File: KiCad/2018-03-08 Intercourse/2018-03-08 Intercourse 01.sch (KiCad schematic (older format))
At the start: 33 parts

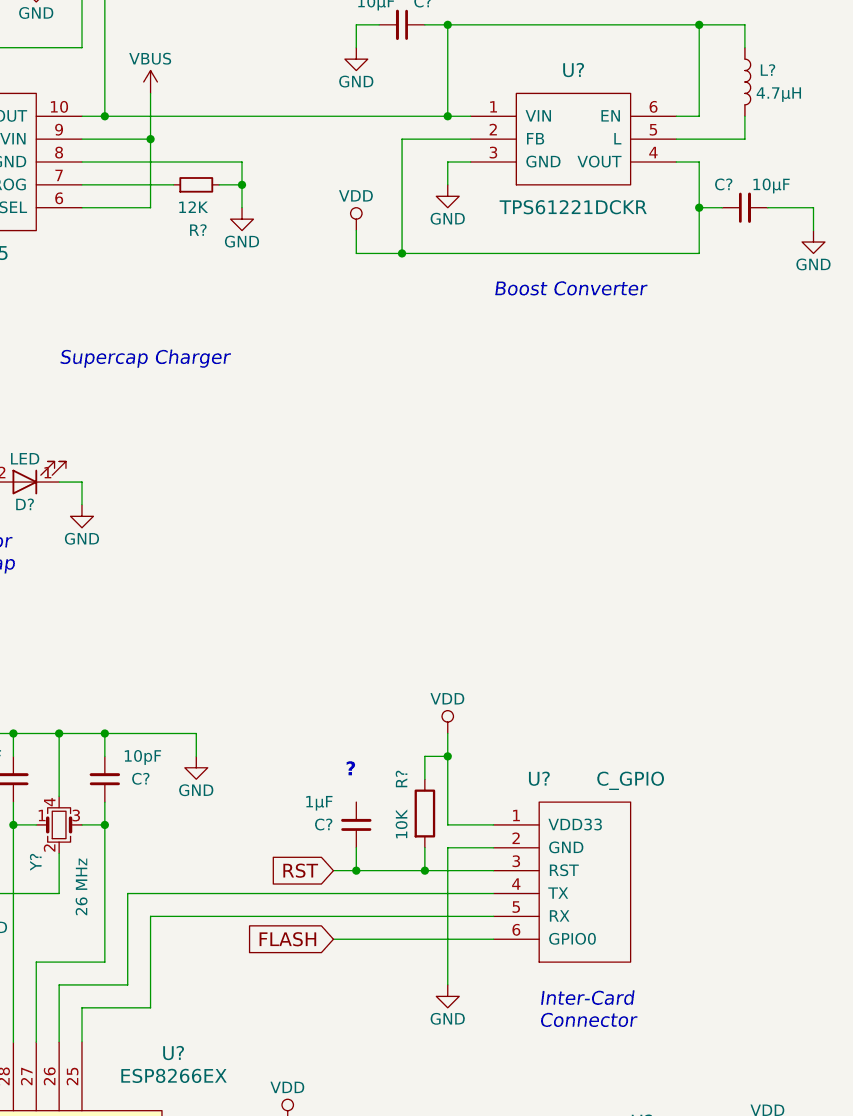
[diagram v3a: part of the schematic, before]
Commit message: added reset rc filter circuit
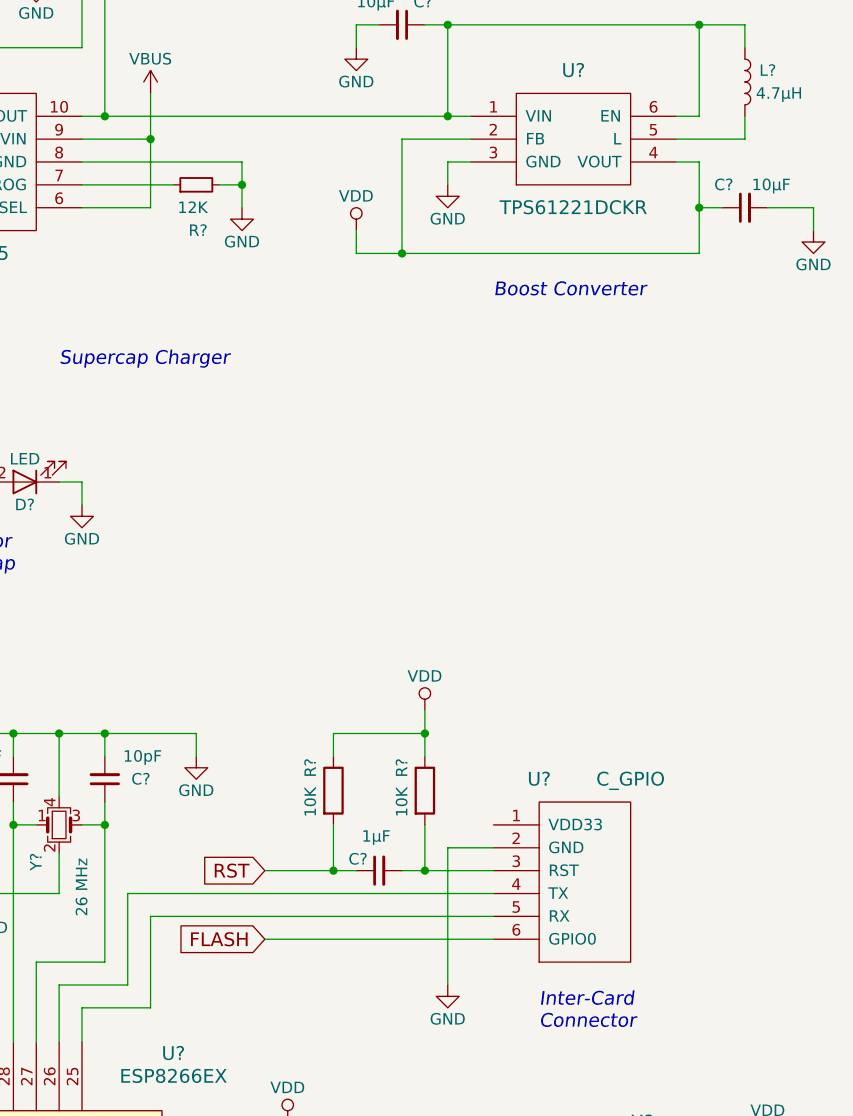
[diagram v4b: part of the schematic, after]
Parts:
- added R?: 10K, symbol R
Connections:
- net RST: now also R?.2; no longer R?.2, U?.3 (RST)
- net VDD: now also R?.1; no longer U?.1 (VDD33)
- net at C?.2: now also R?.2, U?.3 (RST)
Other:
- moved on the sheet: C?, R?
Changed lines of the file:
@@
 Text Notes 1400 6100 2    60   ~ 12
-?
-Text Notes 5200 5200 2    60   ~ 12
 ?
 $Comp
@@
 L VDD #PWR?
 U 1 1 5AB0F171
-P 5600 5000
-F 0 "#PWR?" H 5600 4850 50  0001 C CNN
-F 1 "VDD" H 5600 5150 50  0000 C CNN
-F 2 "" H 5600 5000 50  0001 C CNN
-F 3 "" H 5600 5000 50  0001 C CNN
-	1    5600 5000
+P 5500 4900
+F 0 "#PWR?" H 5500 4750 50  0001 C CNN
+F 1 "VDD" H 5500 5050 50  0000 C CNN
+F 2 "" H 5500 4900 50  0001 C CNN
+F 3 "" H 5500 4900 50  0001 C CNN
+	1    5500 4900
 	1    0    0    -1
 $EndComp
@@
 L R R?
 U 1 1 5AB249C6
-P 5500 5350
-F 0 "R?" V 5400 5500 50  0000 C CNN
-F 1 "10K" V 5400 5300 50  0000 C CNN
-F 2 "" V 5430 5350 50  0001 C CNN
-F 3 "" H 5500 5350 50  0001 C CNN
-	1    5500 5350
+P 5500 5250
+F 0 "R?" V 5400 5350 50  0000 C CNN
+F 1 "10K" V 5400 5200 50  0000 C CNN
+F 2 "" V 5430 5250 50  0001 C CNN
+F 3 "" H 5500 5250 50  0001 C CNN
+	1    5500 5250
 	1    0    0    -1
 $EndComp
@@
 L C_Small C?
 U 1 1 5AB287B2
-P 5200 5400
-F 0 "C?" H 5300 5400 50  0000 L CNN
-F 1 "1μF" H 5300 5300 50  0000 L CNN
-F 2 "" H 5200 5400 50  0001 C CNN
-F 3 "" H 5200 5400 50  0001 C CNN
-	1    5200 5400
-	-1   0    0    1
+P 5300 5600
+F 0 "C?" V 5350 5650 50  0000 L CNN
+F 1 "1μF" V 5450 5550 50  0000 L CNN
+F 2 "" H 5300 5600 50  0001 C CNN
+F 3 "" H 5300 5600 50  0001 C CNN
+	1    5300 5600
+	0    -1   -1   0
 $EndComp
 Wire Wire Line
@@
 	6600 2500 6700 2500
 Wire Wire Line
-	6700 2900 6700 2700
-Wire Wire Line
-	6700 2700 6700 2500
-Wire Wire Line
-	5200 2900 5400 2900
-Wire Wire Line
-	5400 2900 6700 2900
+	6700 2500 6700 2700
+Wire Wire Line
+	6700 2700 6700 2900
+Wire Wire Line
+	6700 2900 5400 2900
+Wire Wire Line
+	5400 2900 5200 2900
 Wire Wire Line
 	5400 2900 5400 2400
@@
 	4200 6100 3900 6100
 Wire Wire Line
-	5600 5400 5800 5400
-Wire Wire Line
 	5600 5500 5800 5500
-Wire Wire Line
-	5100 5600 5200 5600
-Wire Wire Line
-	5200 5600 5500 5600
-Wire Wire Line
-	5500 5600 5800 5600
 Wire Wire Line
 	4200 5700 4200 6100
@@
 	1100 3700 1100 3800
 Wire Wire Line
-	5600 5000 5600 5100
-Wire Wire Line
-	5600 5100 5600 5400
-Wire Wire Line
 	1100 5700 1100 5600
 Wire Wire Line
@@
 	3400 5000 3400 5200
 Wire Wire Line
-	5100 5900 5800 5900
+	4800 5900 5800 5900
 Wire Wire Line
 	4500 5000 4500 5100
@@
 Connection ~ 3200 5700
 Wire Wire Line
-	5200 5600 5200 5500
-Connection ~ 5200 5600
-Wire Wire Line
-	5500 5200 5500 5100
-Wire Wire Line
-	5500 5100 5600 5100
-Connection ~ 5600 5100
-Wire Wire Line
-	5500 5500 5500 5600
-Connection ~ 5500 5600
+	5500 4900 5500 5000
+Wire Wire Line
+	5500 5000 5500 5100
+Wire Wire Line
+	5500 5400 5500 5600
 Wire Wire Line
 	3500 6350 3500 6200
@@
 Text Notes 1400 9200 0    60   Italic 12
 Todo:\n* Status LEDs\n* USB Conn Check\n* Reset
-Text GLabel 5100 5900 0    60   Input ~ 0
+Text GLabel 4800 5900 0    60   Input ~ 0
 FLASH
-Text GLabel 5100 5600 0    60   Input ~ 0
+Text GLabel 4800 5600 0    60   Input ~ 0
 RST
 Text GLabel 4100 8100 2    60   Input ~ 0
@@
 Text GLabel 3300 6200 1    60   Input ~ 0
 RST
+$Comp
+L R R?
+U 1 1 5AB29192
+P 5100 5250
+F 0 "R?" V 5000 5350 50  0000 C CNN
+F 1 "10K" V 5000 5200 50  0000 C CNN
+F 2 "" V 5030 5250 50  0001 C CNN
+F 3 "" H 5100 5250 50  0001 C CNN
+	1    5100 5250
+	1    0    0    -1
+$EndComp
+Wire Wire Line
+	5100 5100 5100 5000
+Wire Wire Line
+	5100 5400 5100 5600
+Wire Wire Line
+	4800 5600 5100 5600
+Wire Wire Line
+	5100 5600 5200 5600
+Connection ~ 5100 5600
+Wire Wire Line
+	5400 5600 5500 5600
+Wire Wire Line
+	5500 5600 5800 5600
+Connection ~ 5500 5600
+Wire Wire Line
+	5100 5000 5500 5000
+Connection ~ 5500 5000
 $EndSCHEMATC

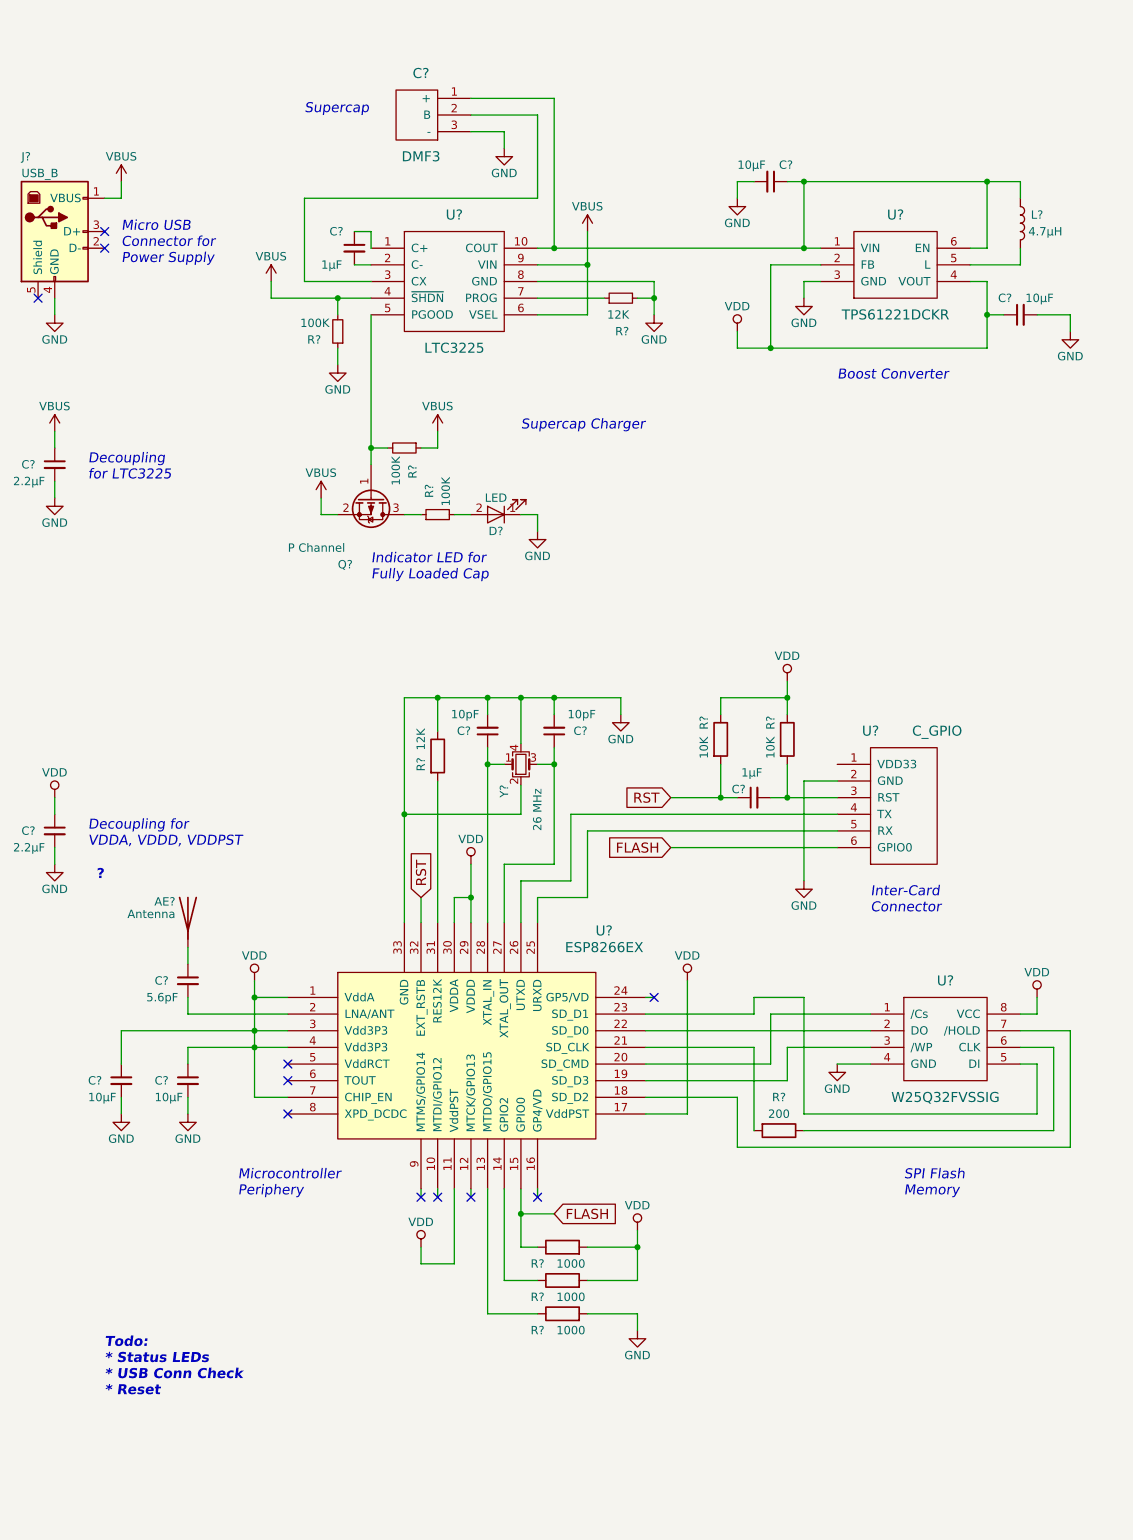
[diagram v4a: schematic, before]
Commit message: added leds to schematic
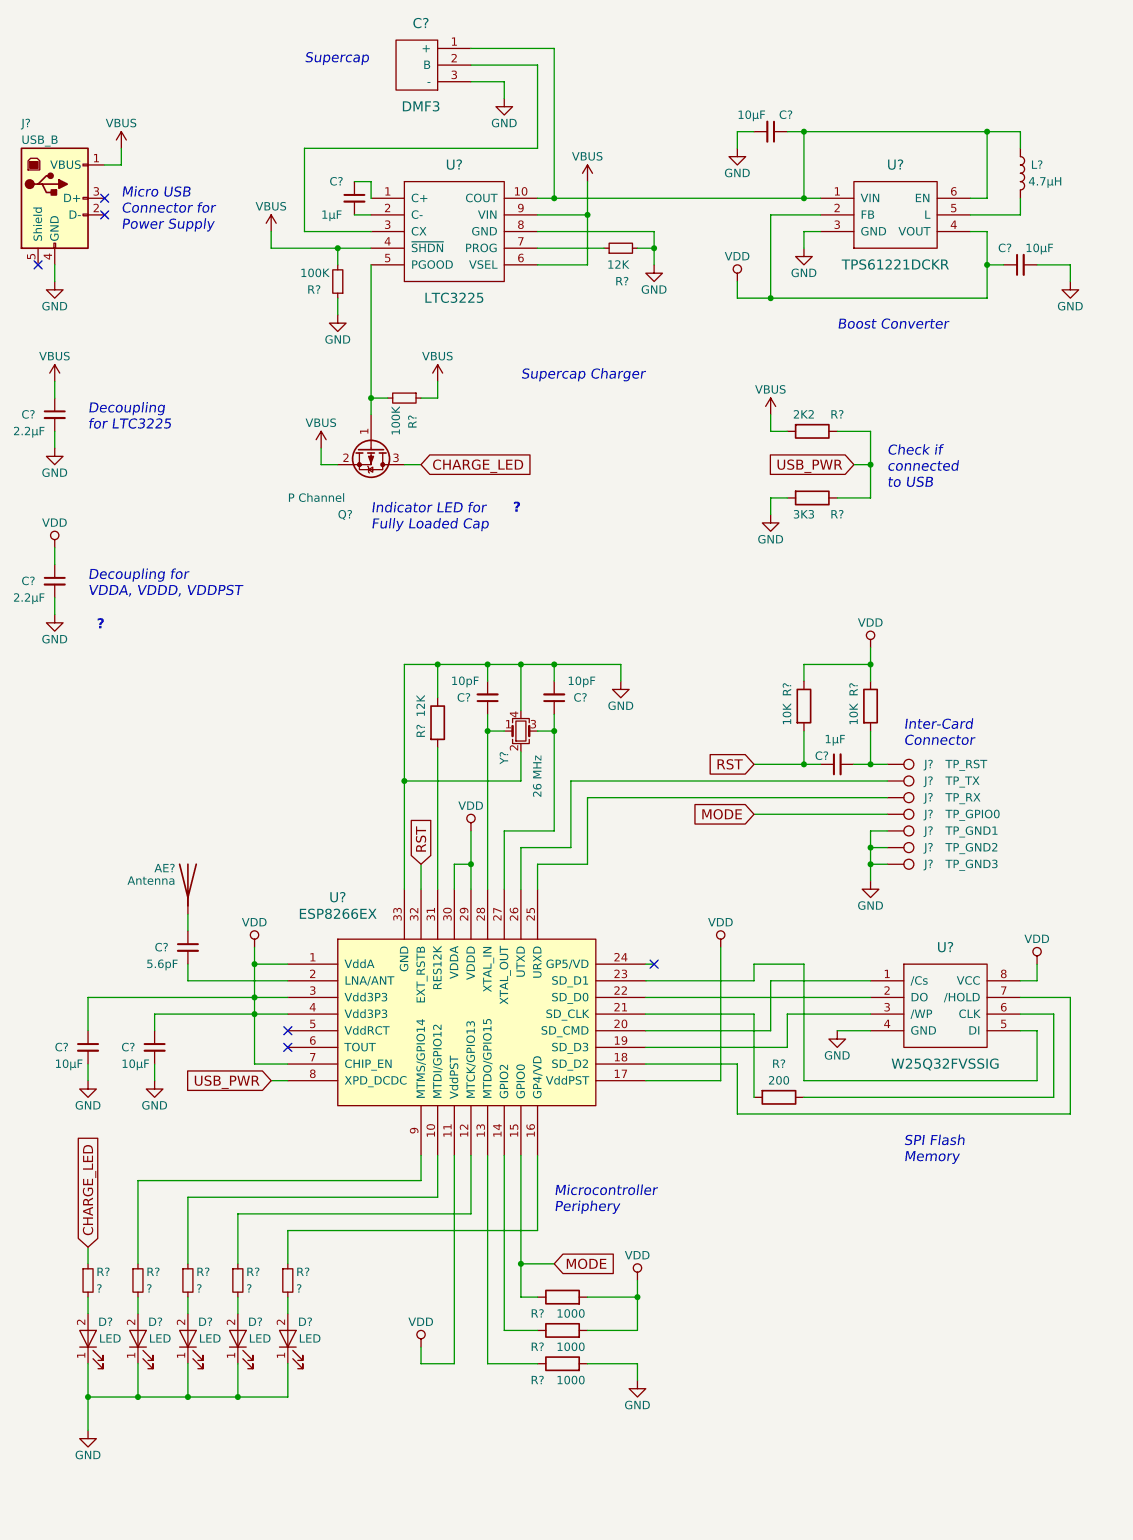
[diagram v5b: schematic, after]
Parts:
- removed U?: C_GPIO, symbol C_GPIO
- added D? (x4): LED, symbol LED
- added J?: TP_TX, symbol TEST_1P
- added J?: TP_GPIO0, symbol TEST_1P
- added J?: TP_RX, symbol TEST_1P
- added J?: TP_RST, symbol TEST_1P
- added J?: TP_GND1, symbol TEST_1P
- added J?: TP_GND2, symbol TEST_1P
- added J?: TP_GND3, symbol TEST_1P
- added R?: 2K2, symbol R
- added R?: 3K3, symbol R
- added R? (x4): ?, symbol R_Small
- R?: value 100K -> ?
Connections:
- net GND: now also D?.1 (K), D?.1 (K), D?.1 (K), D?.1 (K), J?.1, J?.1, J?.1, R?.2
- net VBUS: now also R?.2
- net at R?.1: now also U?.16 (GP4/VD); no longer Q?.3 (D)
- net at U?.10 (MTDI/GPIO12): now also R?.1
- net at U?.12 (MTCK/GPIO13): now also R?.1
- net at U?.25 (URXD): now also J?.1
- net at U?.26 (UTXD): now also J?.1
- net USB_PWR: now reaches U?.8 (XPD_DCDC)
- net USB_PWR: now also R?.1, R?.1
- net at U?.9 (MTMS/GPIO14): now also R?.1
- net at C?.2, R?.2: now also J?.1
- net FLASH renamed MODE
- net MODE: now also J?.1
- new net: D?.2 (A), R?.2 (x4)
- new net CHARGE_LED: Q?.3 (D), R?.1
- no-connect marks 11 -> 6
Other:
- note added: "Check if\nconnected\nto USB"
- note removed: "Todo:\n* Status LEDs\n* USB Conn Check\n* Reset"
- moved on the sheet: AE?, C?, D?, J?, L?, Q?, R?, U?, Y?

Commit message: added usb c recaptable
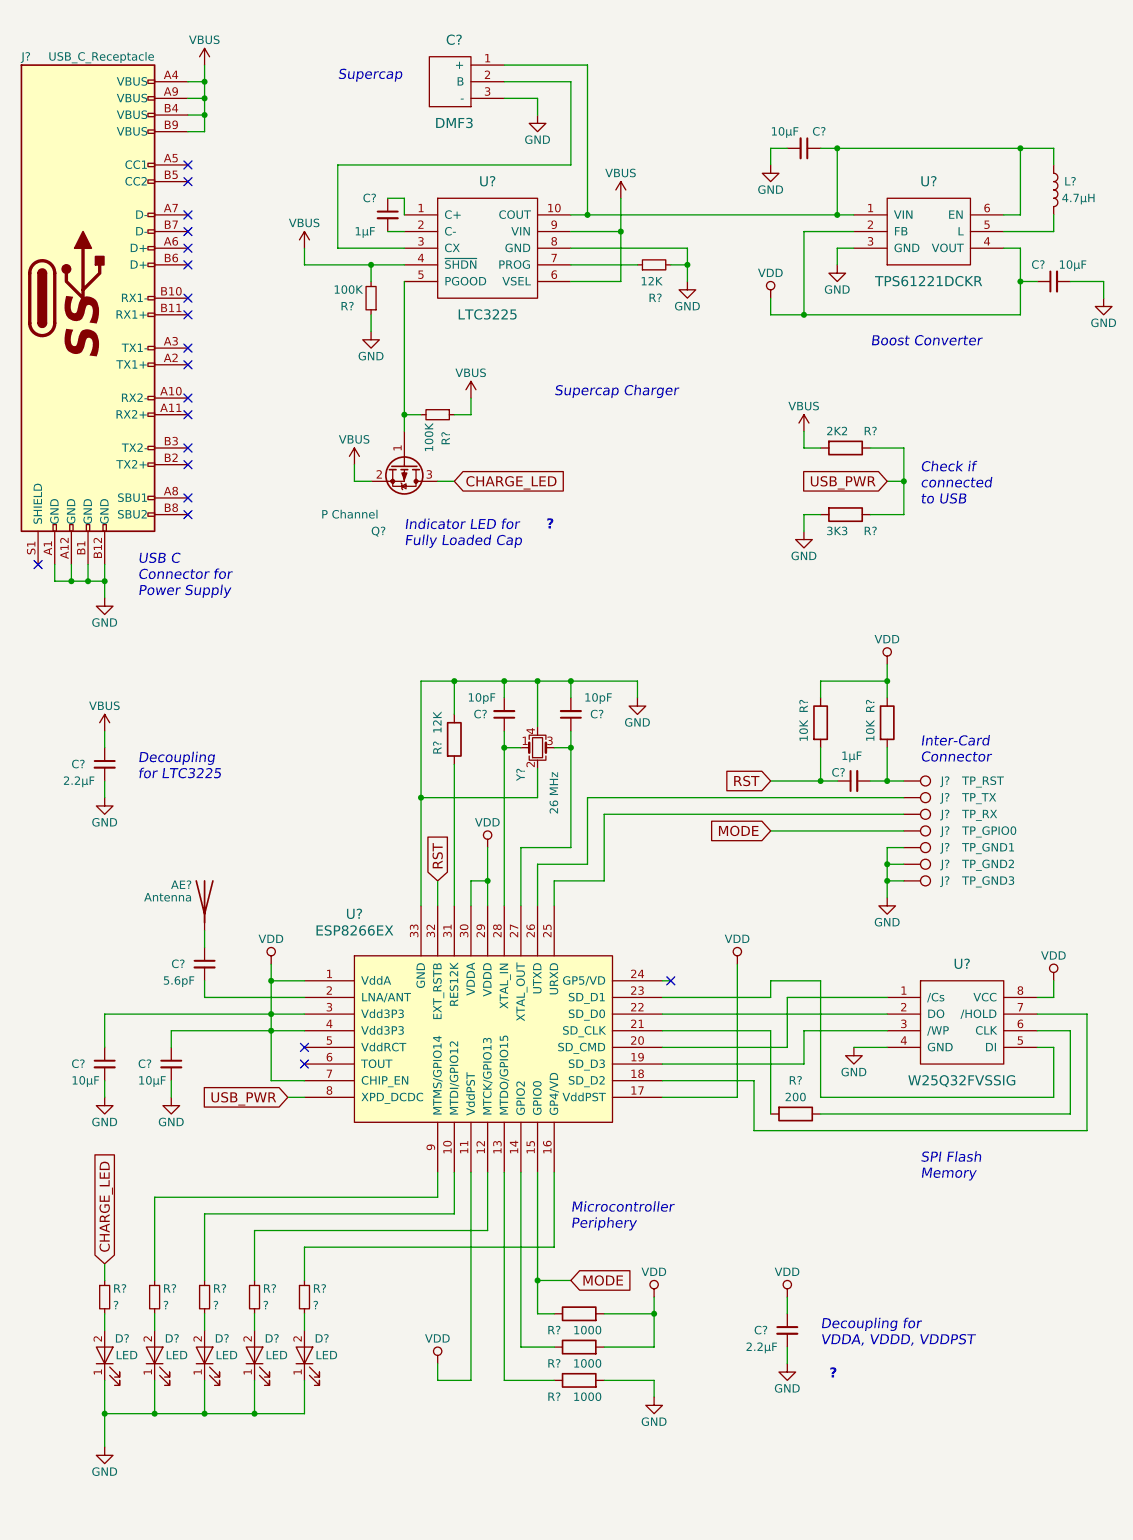
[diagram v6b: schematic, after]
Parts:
- removed J?: USB_B, symbol USB_B
- added J?: USB_C_Receptacle, symbol USB_C_Receptacle
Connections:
- net GND: now also J?.A1 (GND), J?.A12 (GND), J?.B1 (GND), J?.B12 (GND)
- net VBUS: now also J?.A4 (VBUS), J?.A9 (VBUS), J?.B4 (VBUS), J?.B9 (VBUS)
- no-connect marks 6 -> 20
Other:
- note added: "USB C\nConnector for\nPower Supply"
- note removed: "Micro USB\nConnector for\nPower Supply"
- moved on the sheet: AE?, C?, D?, J?, L?, Q?, R?, U?, Y?
